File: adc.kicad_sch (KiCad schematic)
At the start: 18 parts

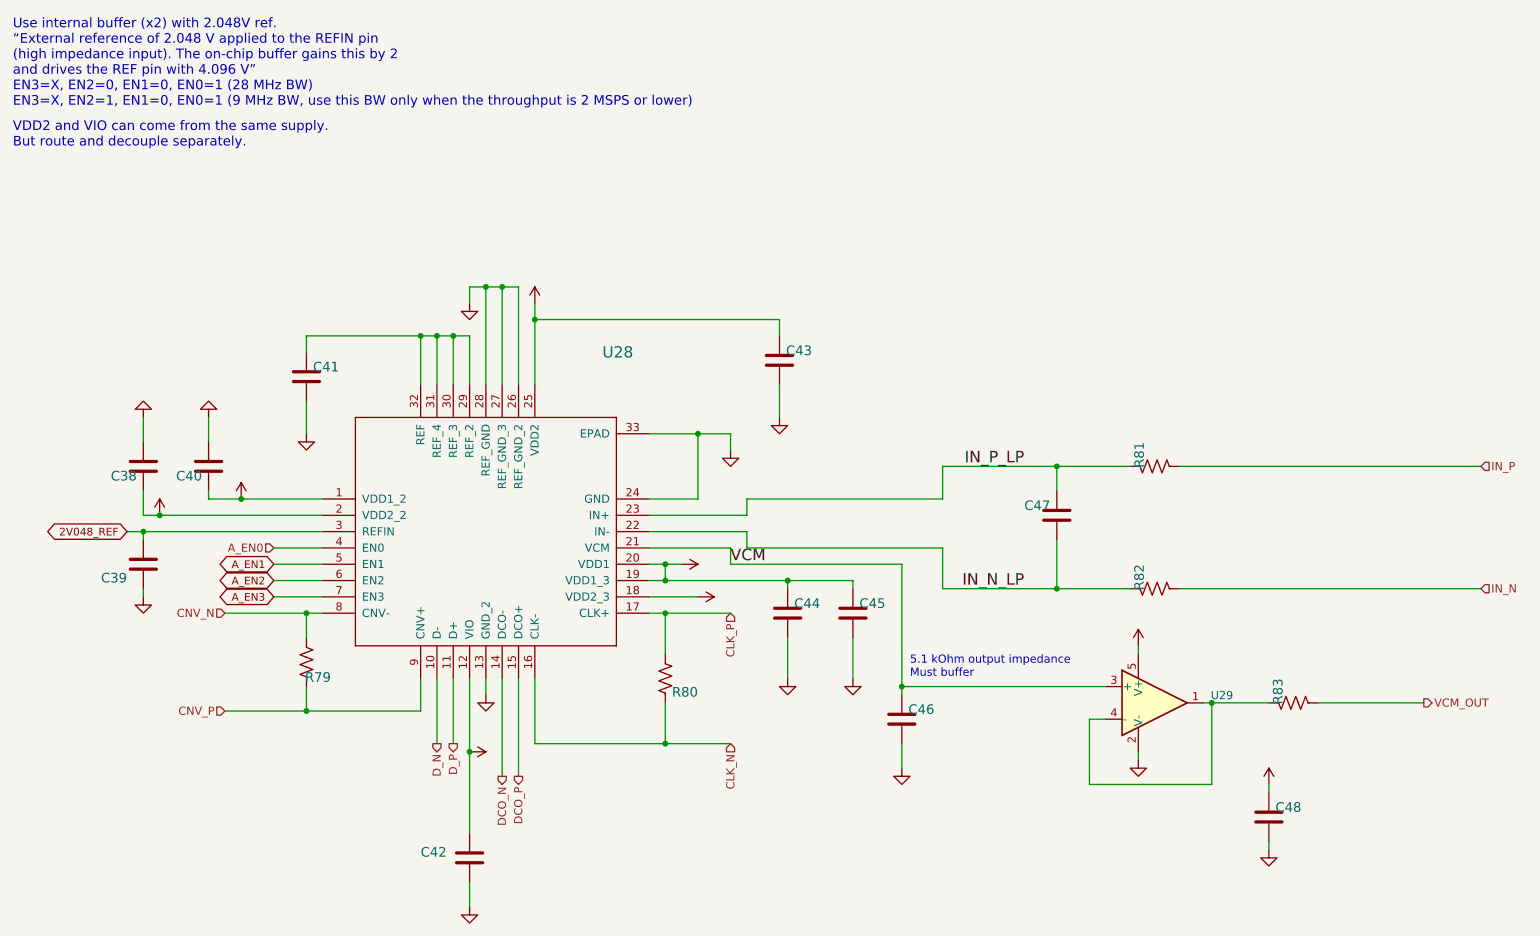
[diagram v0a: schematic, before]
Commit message: closes #31 - incorrect text on Howland current pump. Also, updated fast DAC symbol but not closing until layout is corrected
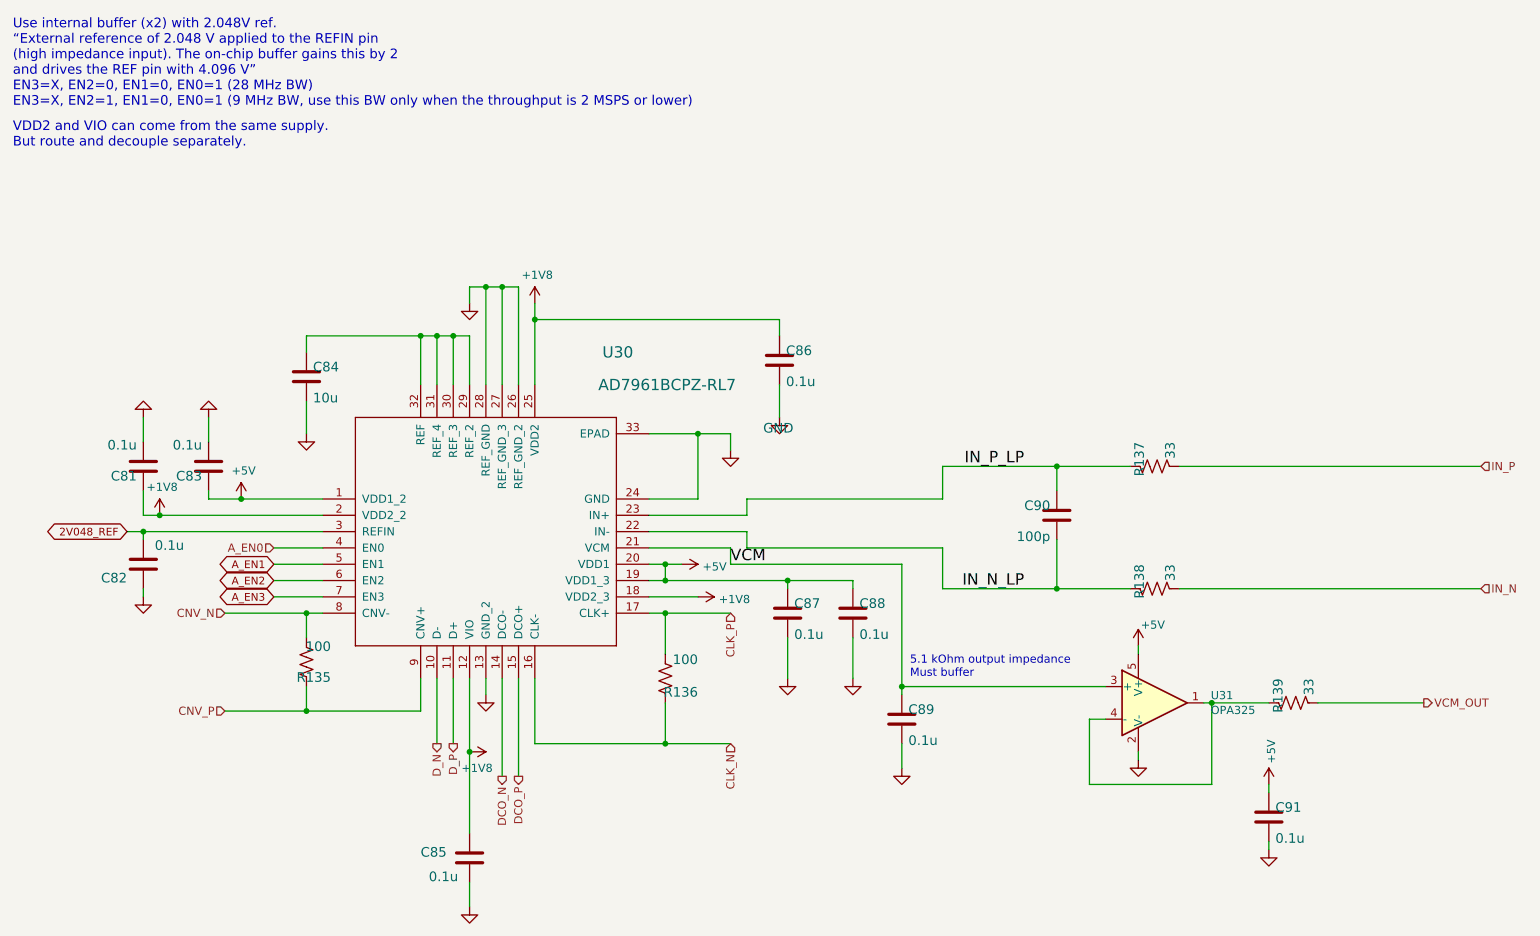
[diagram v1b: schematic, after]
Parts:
- C81: renamed from C38; value (none) -> 0.1u; footprint (none) -> Capacitor_SMD:C_0603_1608Metric
- C82: renamed from C39; value (none) -> 0.1u; footprint (none) -> Capacitor_SMD:C_0603_1608Metric
- C83: renamed from C40; value (none) -> 0.1u; footprint (none) -> Capacitor_SMD:C_0603_1608Metric
- C84: renamed from C41; value (none) -> 10u; footprint (none) -> Capacitor_SMD:C_0603_1608Metric
- C85: renamed from C42; value (none) -> 0.1u; footprint (none) -> Capacitor_SMD:C_0603_1608Metric
- C86: renamed from C43; value (none) -> 0.1u; footprint (none) -> Capacitor_SMD:C_0603_1608Metric
- C87: renamed from C44; value (none) -> 0.1u; footprint (none) -> Capacitor_SMD:C_0603_1608Metric
- C88: renamed from C45; value (none) -> 0.1u; footprint (none) -> Capacitor_SMD:C_0603_1608Metric
- C89: renamed from C46; value (none) -> 0.1u; footprint (none) -> Capacitor_SMD:C_0603_1608Metric
- C90: renamed from C47; value (none) -> 100p; footprint (none) -> Capacitor_SMD:C_0603_1608Metric
- C91: renamed from C48; value (none) -> 0.1u; footprint (none) -> Capacitor_SMD:C_0603_1608Metric
- R135: renamed from R79; value (none) -> 100; footprint (none) -> Resistor_SMD:R_0603_1608Metric
- R136: renamed from R80; value (none) -> 100; footprint (none) -> Resistor_SMD:R_0603_1608Metric
- R137: renamed from R81; value (none) -> 33; footprint (none) -> Resistor_SMD:R_0603_1608Metric
- R138: renamed from R82; value (none) -> 33; footprint (none) -> Resistor_SMD:R_0603_1608Metric
- R139: renamed from R83; value (none) -> 33; footprint (none) -> Resistor_SMD:R_0603_1608Metric
- U30: renamed from U28; value (none) -> AD7961BCPZ-RL7; footprint (none) -> Package_DFN_QFN:QFN-32-1EP_5x5mm_P0.5mm_EP3.1x3.1mm
- U31: renamed from U29; value (none) -> OPA325; footprint (none) -> Package_TO_SOT_SMD:SOT-23-5
